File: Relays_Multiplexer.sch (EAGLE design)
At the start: 89 parts, among them IC1 PCA9685, IC2 PCA9685, J1 PTH VERT MALE, J2 1x33 Molex Connector, J3 PTH VERT FEMALE, J4 PTH VERT FEMALE, J5 2x17 PTH RA FEMALE

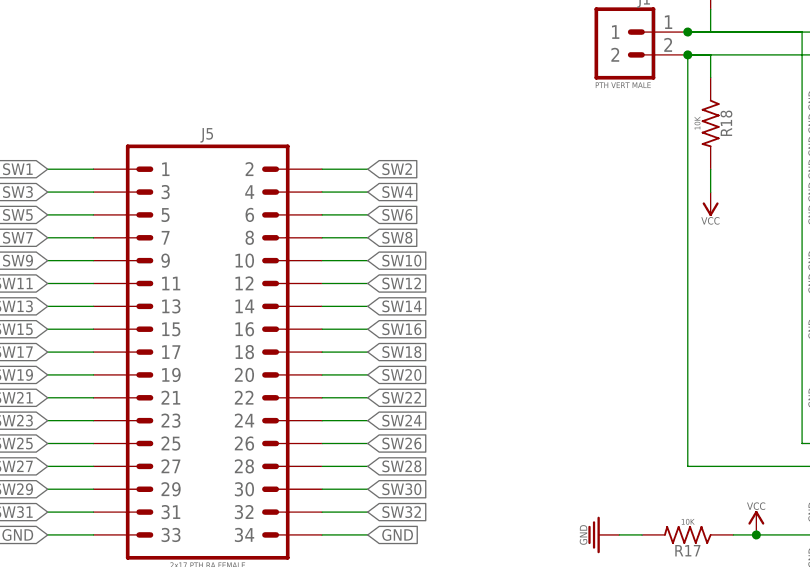
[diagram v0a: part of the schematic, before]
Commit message: Board is fully routed, but kind of looks like shit
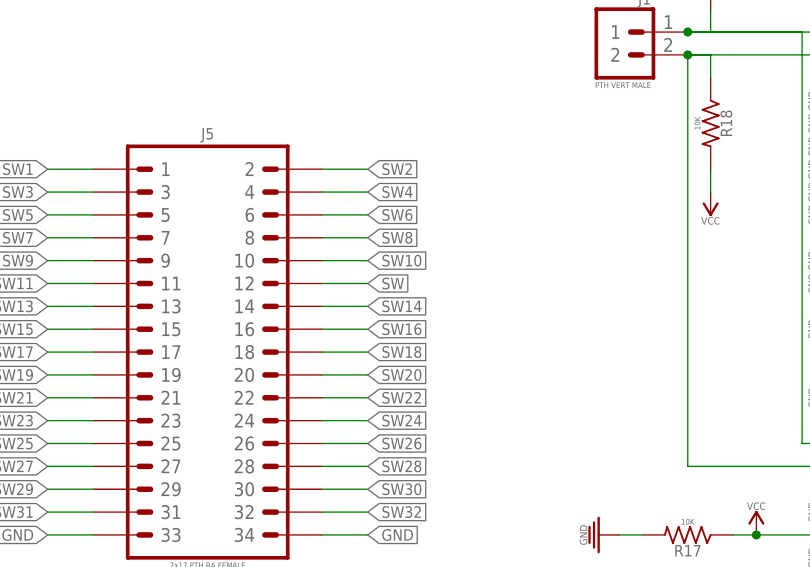
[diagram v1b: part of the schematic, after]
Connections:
- net SW12 renamed SW
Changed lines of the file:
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@@
 </segment>
 </net>
-<net name="SW12" class="0">
+<net name="SW" class="0">
 <segment>
 <pinref part="IC1" gate="G$1" pin="PWM11"/>

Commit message: Board is fully routed. We out here finishing things
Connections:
- net N$13 renamed SDA
- net N$14 renamed SCL
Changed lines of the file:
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@@
 </segment>
 </net>
-<net name="N$13" class="0">
+<net name="SDA" class="0">
 <segment>
 <pinref part="R4" gate="G$1" pin="2"/>
@@
 </segment>
 </net>
-<net name="N$14" class="0">
+<net name="SCL" class="0">
 <segment>
 <pinref part="J1" gate="G$1" pin="2"/>

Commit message: Board is fully routed. We out here finishing things part 2
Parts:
- J1: value PTH VERT MALE -> PTH VERT FEMALE; device _connectors:1X02_PTH_VERT_MALE_2.54MM -> _connectors:1X02_PTH_VERT_FEMALE_2.54MM
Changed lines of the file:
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@@
 <part name="C2" library="_capacitors" deviceset="10UF" device="_CER_SMD-0402_6.3V-20%" package3d_urn="urn:adsk.eagle:package:2886515/1" value="10uF/6.3V"/>
 <part name="SUPPLY24" library="_power_symbols" deviceset="GND" device=""/>
-<part name="J1" library="_connectors" deviceset="1X02" device="_PTH_VERT_MALE_2.54MM" package3d_urn="urn:adsk.eagle:package:4781708/8" value="PTH VERT MALE"/>
+<part name="J1" library="_connectors" deviceset="1X02" device="_PTH_VERT_FEMALE_2.54MM" package3d_urn="urn:adsk.eagle:package:4781720/1" value="PTH VERT FEMALE"/>
 <part name="R4" library="_resistors" deviceset="10KΩ" device="_SMD-0402_1/16W-5%" package3d_urn="urn:adsk.eagle:package:2899165/1" value="10K"/>
 <part name="SUPPLY25" library="_power_symbols" deviceset="VCC" device=""/>
